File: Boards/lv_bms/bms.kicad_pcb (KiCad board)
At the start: 4 copper layers, 109.3 x 58.3 mm, 89 parts, among them J1 CONN_02X03, SW1 SW_Push_SPST_NO, U1 MCP2561-E_SN, U101 TPS560430YF, U14 LR8K4-G, U2 ATMEGA16M1, U3 BQ79606A-Q1, Y1 Crystal_SMD

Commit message: some partial layout changes
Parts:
- moved R4 12.1 mm to (154.0, 107.2)
- moved C16 7.74 mm to (149.1, 113.8)
- moved D1 7.61 mm to (157.7, 104.1)
- moved C21 6.69 mm to (139.5, 111.5)
- moved C26 6.56 mm to (144.5, 113.5), turned to 180 degrees
- moved R19 5.49 mm to (158.1, 107.2)
- moved R5 5.38 mm to (158.1, 110.5)
- moved R6 4.83 mm to (154.0, 110.5)
- moved R15 4.13 mm to (158.1, 113.8), turned to 0 degrees
- moved C17 2.28 mm to (139.7, 113.5)
- moved C18 1.97 mm to (137.7, 115.3)
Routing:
- net /UARTTX: track 13.1 -> 43.9 mm, vias 3 -> 6
- net VCC: track 128.3 -> 154.9 mm
- net /VIO: track 31.0 -> 51.2 mm, vias 2 -> 8
- net Net-(C21-Pad2): track 1.90 -> 21.8 mm, vias 0 -> 2
- net /WAKEUP: track 21.4 -> 38.6 mm, vias 4 -> 8
- net /BattConn4: track 48.2 -> 65.2 mm, vias 2 -> 4
- net GNDA: track 78.1 -> 91.2 mm, vias 16 -> 18
- net Net-(D1-Pad2): track 4.50 -> 16.0 mm, vias 0 -> 2
- net /UARTRX: track 12.8 -> 23.1 mm, vias 3 -> 4
- net Net-(R5-Pad2): track 8.76 -> 16.3 mm, vias 0 -> 2
- net Net-(C16-Pad1): track 2.95 -> 10.5 mm, vias 0 -> 2
- net /NFAULT: track 16.4 -> 21.5 mm, vias 4 -> 0
- net /REF1: track 0.89 -> 5.41 mm
- net /GPIO5: track 16.1 -> 13.5 mm
- net /AVDD: track 0.00 -> 2.38 mm
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
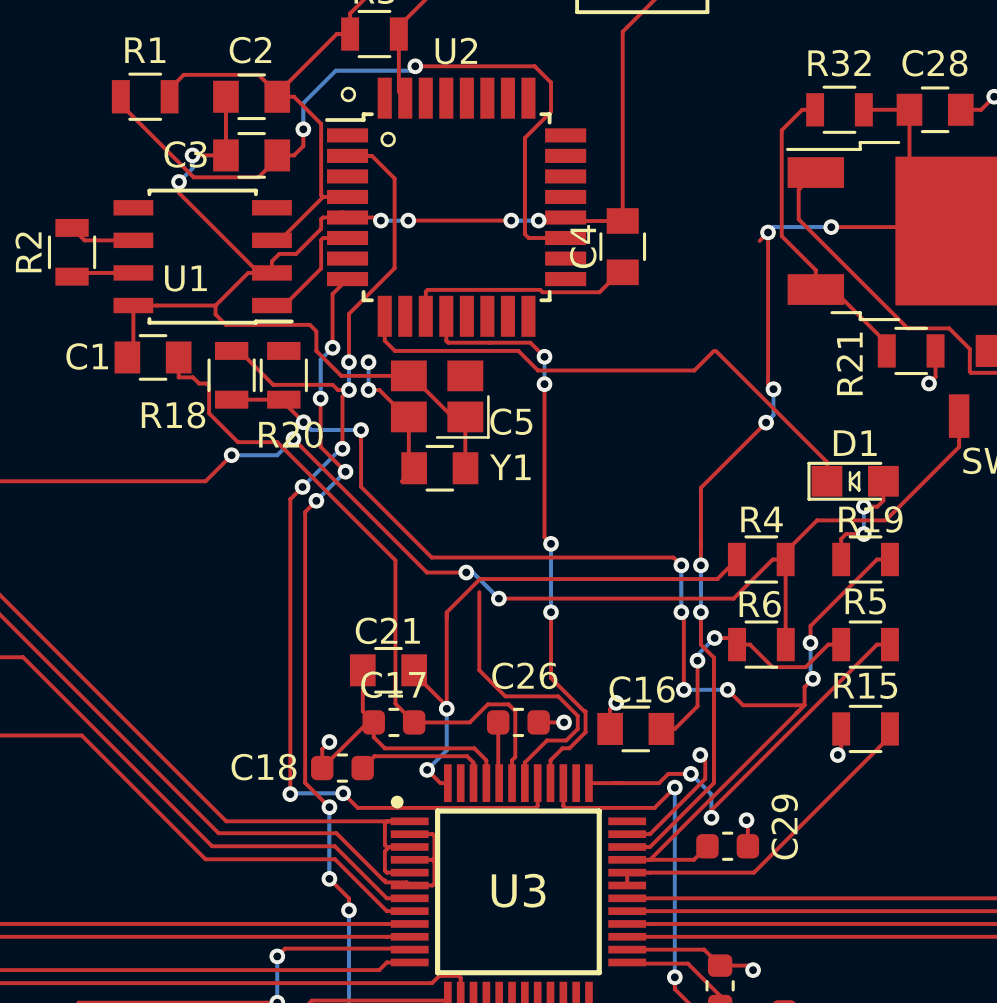
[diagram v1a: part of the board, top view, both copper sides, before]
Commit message: fixed general spacing issues, bypass capacitor spacing, CAN Tranciever spacing / vias & crystal spacing / vias
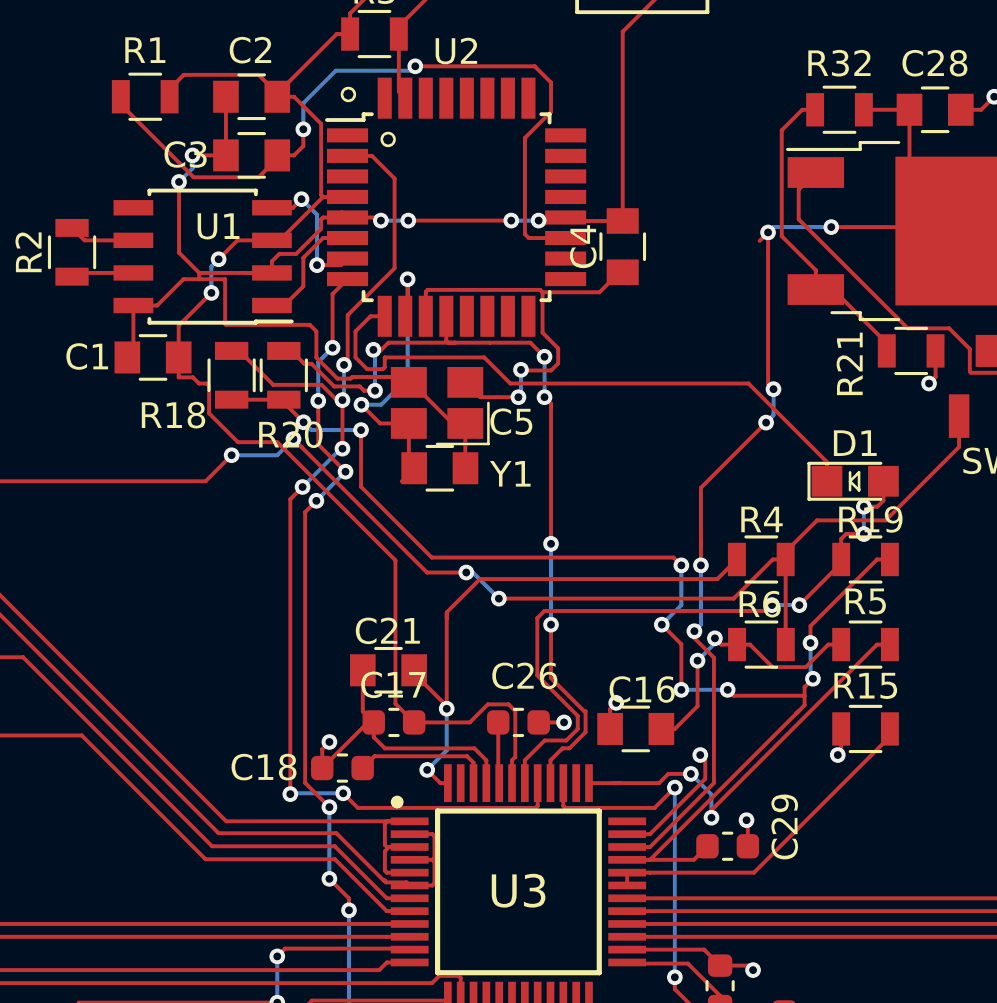
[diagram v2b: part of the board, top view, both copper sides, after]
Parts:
- moved Y1 0.25 mm to (141.4, 101.1)
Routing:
- net Net-(D1-Pad2): track 16.0 -> 25.7 mm, vias 2 -> 4
- net /UARTRX: track 23.1 -> 32.2 mm, vias 4 -> 6
- net Net-(C4-Pad1): track 9.12 -> 17.6 mm, vias 0 -> 2
- net VCC: track 154.9 -> 161.7 mm, vias 2 -> 4
- net Net-(C5-Pad1): track 6.08 -> 12.6 mm
- net /CAN_RX: track 0.06 -> 6.18 mm, vias 0 -> 2
- net /NFAULT: track 21.5 -> 23.8 mm
- net GND: track 130.8 -> 132.3 mm
- net /VIO: track 51.2 -> 51.7 mm

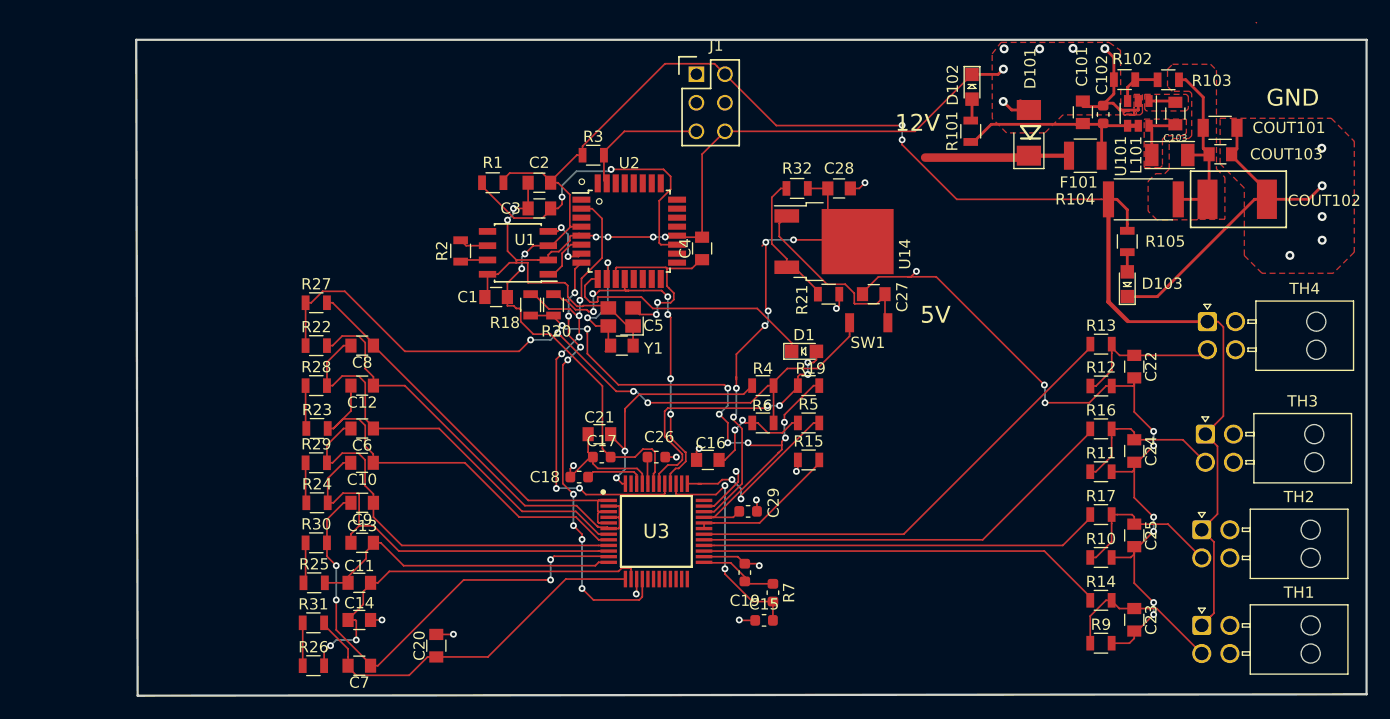
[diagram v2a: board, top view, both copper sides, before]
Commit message: almost all layout fixes except footprint screw terminal footprint
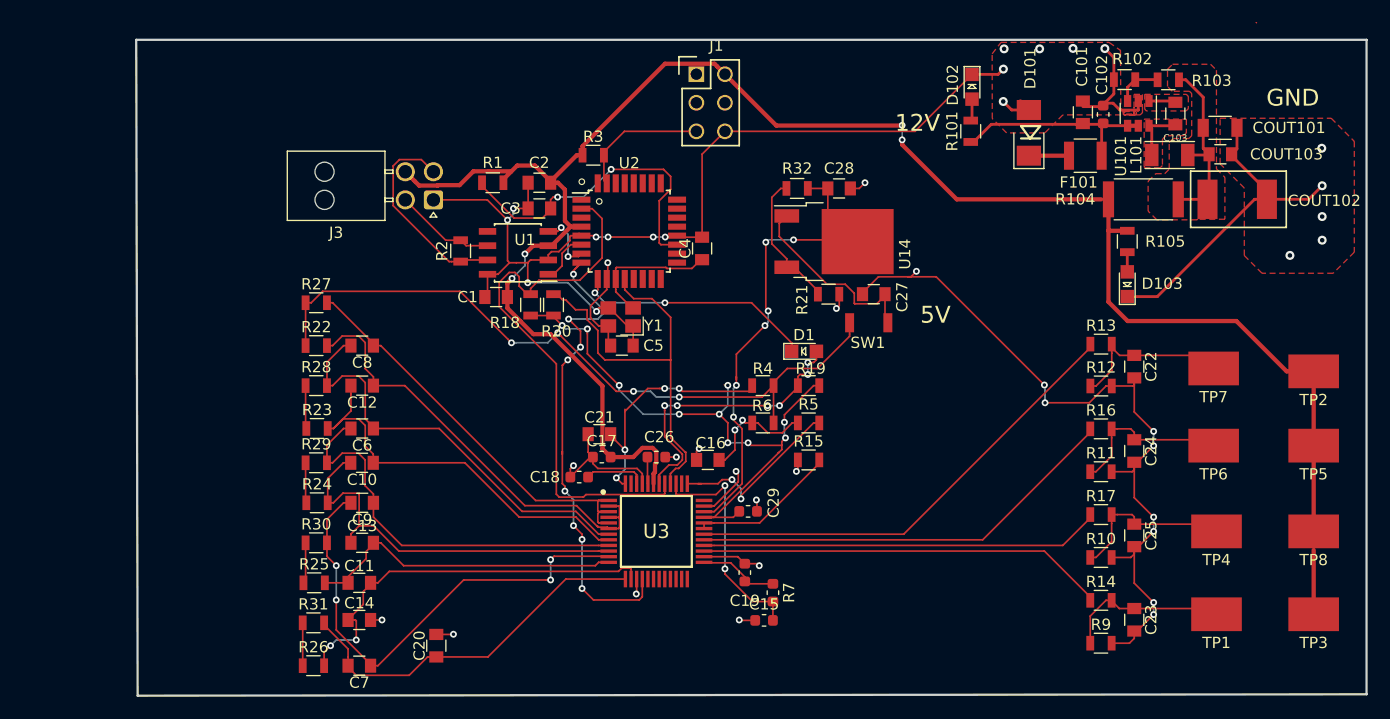
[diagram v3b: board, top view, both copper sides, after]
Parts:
- removed TH1, TH2, TH3, TH4: Thermistor, footprints:NanoFit_RA_4
- added J3: NanoFit_RA_04, footprints:NanoFit_RA_4, F.Cu at (124.7, 90.7)
- added TP1: Test_Point_SMD, footprints:Test_Point_SMD, F.Cu at (194.3, 127.5)
- added TP2: Test_Point_SMD, footprints:Test_Point_SMD, F.Cu at (202.9, 105.9)
- added TP3: Test_Point_SMD, footprints:Test_Point_SMD, F.Cu at (202.9, 127.5)
- added TP4: Test_Point_SMD, footprints:Test_Point_SMD, F.Cu at (194.3, 120.1)
- added TP5: Test_Point_SMD, footprints:Test_Point_SMD, F.Cu at (202.9, 112.5)
- added TP6: Test_Point_SMD, footprints:Test_Point_SMD, F.Cu at (194.1, 112.5)
- added TP7: Test_Point_SMD, footprints:Test_Point_SMD, F.Cu at (194.1, 105.7)
- added TP8: Test_Point_SMD, footprints:Test_Point_SMD, F.Cu at (202.9, 120.1)
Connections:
- net Net-(C22-Pad1) renamed /-Therm4SMD
- net Net-(C23-Pad1) renamed /-Therm1SMD
- net Net-(C24-Pad1) renamed /-Therm3SMD
- net Net-(C25-Pad1) renamed /-Therm2SMD
- D101 pad 1: (no net) -> Net-(C101-Pad1)
- F101 pad 2: (no net) -> /BattConn4
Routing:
- net /CAN_HI: track 2.45 -> 18.3 mm
- net VCC: track 161.7 -> 172.5 mm
- net (no net): track 12.9 -> 3.87 mm
- net /CAN_LO: track 2.59 -> 8.99 mm
- net /UARTTX: track 43.8 -> 50.1 mm, vias 6 -> 0
- net Net-(C4-Pad1): track 17.6 -> 12.3 mm, vias 2 -> 0
- net /WAKEUP: track 38.7 -> 43.5 mm
- net GND: track 132.3 -> 136.9 mm, vias 17 -> 19
- net /UARTRX: track 32.2 -> 36.7 mm, vias 6 -> 0
- net Net-(C5-Pad1): track 12.6 -> 9.47 mm, vias 2 -> 1
- net /NFAULT: track 23.8 -> 21.4 mm, vias 0 -> 2
- net /BattConn4: track 65.2 -> 64.1 mm
- net /VIO: track 51.7 -> 52.7 mm, vias 8 -> 10
- net /-Therm4SMD: track 14.1 -> 14.9 mm
- net Net-(C3-Pad1): track 29.3 -> 28.8 mm
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- removed copper zone on In2.Cu, net GNDD
- removed copper zone on In2.Cu, net GNDPWR

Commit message: minor layout changes
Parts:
- J3: value NanoFit_RA_04 -> NanoFit_RA_TH_04
- moved J3 0.11 mm to (124.6, 90.7)

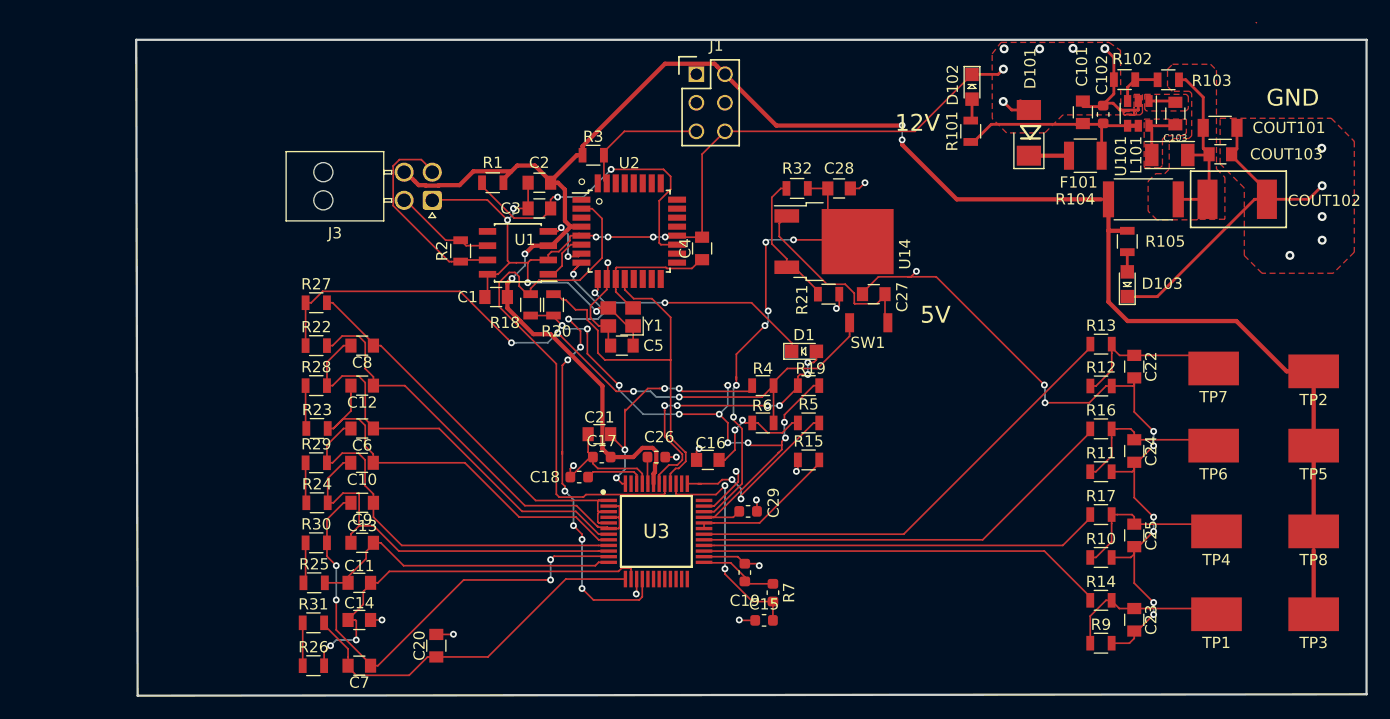
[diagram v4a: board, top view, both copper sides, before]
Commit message: added in screw terminal footprint to layout
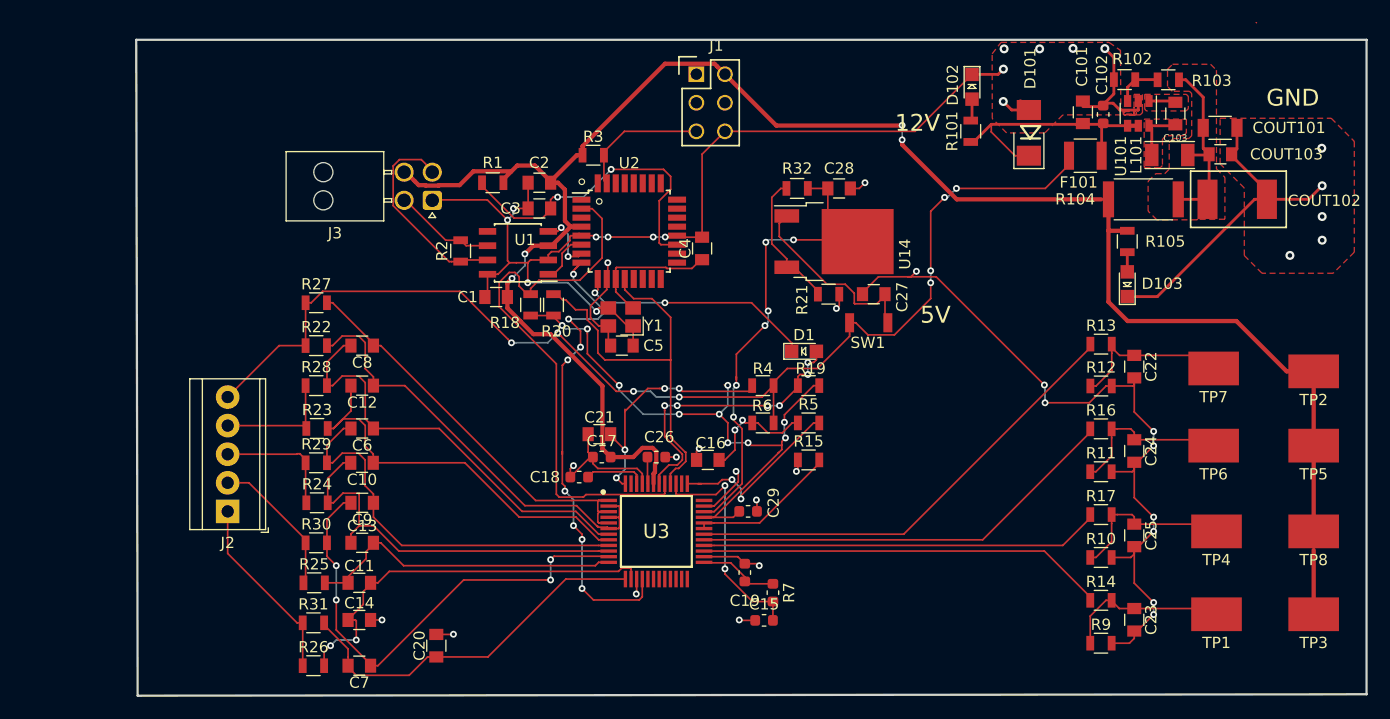
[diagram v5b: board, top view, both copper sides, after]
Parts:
- added J2: Screw_Terminal_01x05, TerminalBlock_TE-Connectivity:TerminalBlock_TE_282834-5_1x05_P2.54mm_Horizontal, F.Cu at (106.4, 118.4)
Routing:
- net /BattConn4: track 64.1 -> 104.5 mm, vias 4 -> 8
- net /BattConn0: track 3.81 -> 16.8 mm
- net /BattConn1: track 3.63 -> 12.9 mm
- net /BattConn2: track 3.58 -> 11.0 mm
- net /BattConn3: track 3.84 -> 10.9 mm
- net Net-(C101-Pad1): track 18.1 -> 23.3 mm
- net (no net): track 3.87 -> 0.00 mm
- added copper zone on In2.Cu, net GNDD
- added copper zone on In2.Cu, net GNDPWR

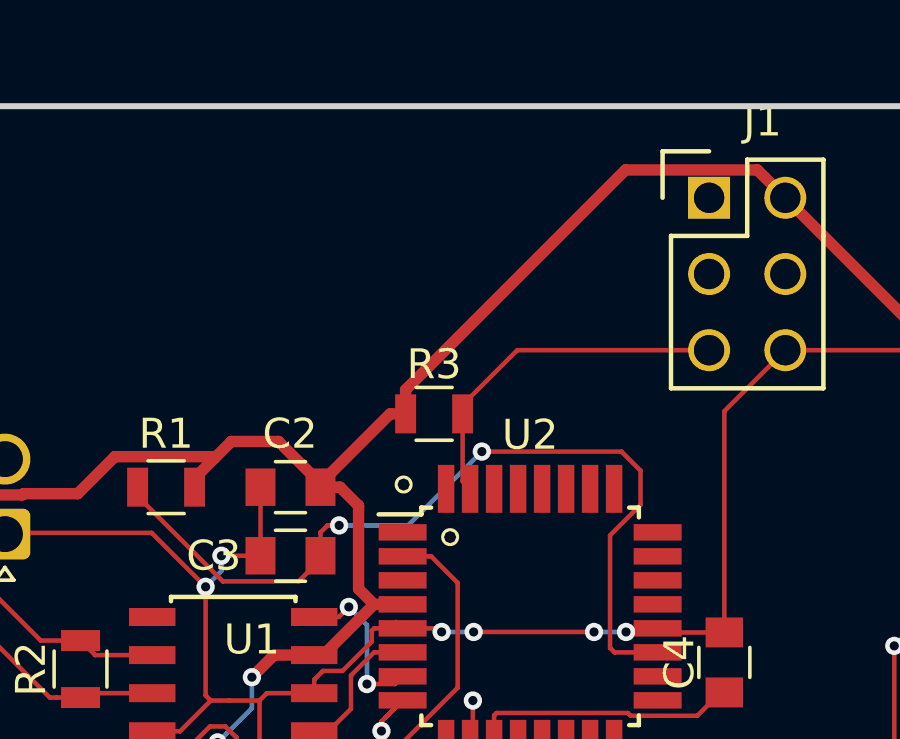
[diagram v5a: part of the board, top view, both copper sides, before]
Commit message: added some debug LEDs
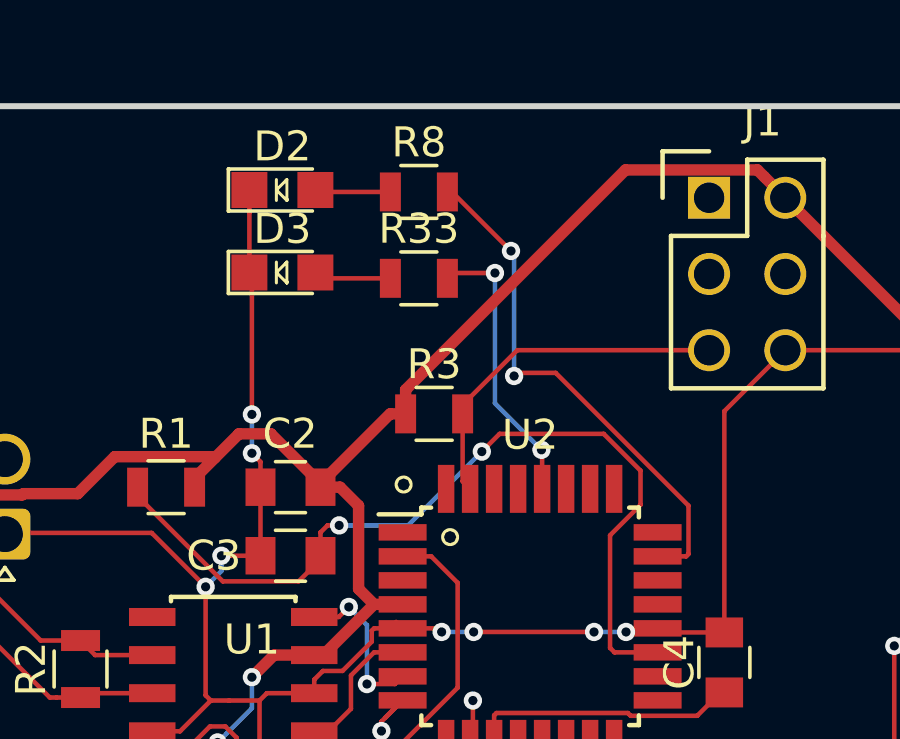
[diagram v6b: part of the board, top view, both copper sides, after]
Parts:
- added D2: LED_0805, footprints:LED_0805_OEM, F.Cu at (133.9, 79.2)
- added D3: LED_0805, footprints:LED_0805_OEM, F.Cu at (133.9, 82.0)
- added R33: R_200, footprints:R_0805_OEM, F.Cu at (138.4, 82.2)
- added R8: R_200, footprints:R_0805_OEM, F.Cu at (138.4, 79.3)
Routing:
- net Net-(R8-Pad2): track 0.00 -> 17.5 mm, vias 0 -> 2
- net GND: track 136.9 -> 146.9 mm, vias 19 -> 21
- net Net-(R33-Pad2): track 0.00 -> 9.51 mm, vias 0 -> 2
- net Net-(D3-Pad2): track 0.00 -> 2.58 mm
- net Net-(D2-Pad2): track 0.00 -> 2.53 mm
